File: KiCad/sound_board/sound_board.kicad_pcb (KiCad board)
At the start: 2 copper layers, 67.3 x 29.2 mm, 16 parts, among them P101 CONN_01X06, P102 CONN_01X06, P103 CONN_01X06, U101 MCP45HVx1, U102 MCP45HVx1, U103 DS1808

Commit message: Gerber
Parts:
- moved REF** 66.0 mm to (205.7, 109.2)
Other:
- board size 67.3 x 29.2 mm -> 65.4 x 26.7 mm
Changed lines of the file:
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@@
     (links 61)
     (no_connects 0)
-    (area 134.544999 93.904999 202.005001 123.265001)
+    (area 142.286667 86.265 221.233334 121.575)
     (thickness 1.6)
     (drawings 6)
@@
     (descr "Through hole straight pin header, 1x06, 2.54mm pitch, single row")
     (tags "Through hole pin header THT 1x06 2.54mm single row")
-    (fp_text reference P103 (at 0 2.39 270) (layer B.SilkS)
+    (fp_text reference P103 (at 0 -15.24 270) (layer B.SilkS)
       (effects (font (size 1 1) (thickness 0.15)) (justify mirror))
     )
@@
   )
   (module Mounting_Holes:MountingHole_3.2mm_M3_Pad (layer F.Cu)
-    (at 139.7 109.22)
+    (at 205.74 109.22)
     (descr "Mounting Hole 3.2mm, M3")
     (tags "mounting hole 3.2mm m3")
@@
     (pad 1 thru_hole circle (at 0 0) (size 6.4 6.4) (drill 3.2) (layers *.Cu *.Mask))
   )
-  (dimension 67.31 (width 0.25) (layer Cmts.User)
-    (gr_text "67,310 mm" (at 168.275 129.27) (layer Cmts.User)
+  (dimension 65.405 (width 0.25) (layer Cmts.User)
+    (gr_text "65,405 mm" (at 176.8475 87.265) (layer Cmts.User)
       (effects (font (size 1 1) (thickness 0.25)))
     )
-    (feature1 (pts (xy 201.93 123.19) (xy 201.93 130.27)))
-    (feature2 (pts (xy 134.62 123.19) (xy 134.62 130.27)))
-    (crossbar (pts (xy 134.62 128.27) (xy 201.93 128.27)))
-    (arrow1a (pts (xy 201.93 128.27) (xy 200.803496 128.856421)))
-    (arrow1b (pts (xy 201.93 128.27) (xy 200.803496 127.683579)))
-    (arrow2a (pts (xy 134.62 128.27) (xy 135.746504 128.856421)))
-    (arrow2b (pts (xy 134.62 128.27) (xy 135.746504 127.683579)))
-  )
-  (dimension 29.21 (width 0.25) (layer Cmts.User)
-    (gr_text "29,210 mm" (at 208.01 108.585 270) (layer Cmts.User)
+    (feature1 (pts (xy 209.55 94.615) (xy 209.55 86.265)))
+    (feature2 (pts (xy 144.145 94.615) (xy 144.145 86.265)))
+    (crossbar (pts (xy 144.145 88.265) (xy 209.55 88.265)))
+    (arrow1a (pts (xy 209.55 88.265) (xy 208.423496 88.851421)))
+    (arrow1b (pts (xy 209.55 88.265) (xy 208.423496 87.678579)))
+    (arrow2a (pts (xy 144.145 88.265) (xy 145.271504 88.851421)))
+    (arrow2b (pts (xy 144.145 88.265) (xy 145.271504 87.678579)))
+  )
+  (dimension 26.67 (width 0.25) (layer Cmts.User)
+    (gr_text "26,670 mm" (at 216.9 107.95 270) (layer Cmts.User)
       (effects (font (size 1 1) (thickness 0.25)))
     )
-    (feature1 (pts (xy 201.93 123.19) (xy 209.01 123.19)))
-    (feature2 (pts (xy 201.93 93.98) (xy 209.01 93.98)))
-    (crossbar (pts (xy 207.01 93.98) (xy 207.01 123.19)))
-    (arrow1a (pts (xy 207.01 123.19) (xy 206.423579 122.063496)))
-    (arrow1b (pts (xy 207.01 123.19) (xy 207.596421 122.063496)))
-    (arrow2a (pts (xy 207.01 93.98) (xy 206.423579 95.106504)))
-    (arrow2b (pts (xy 207.01 93.98) (xy 207.596421 95.106504)))
-  )
-  (gr_line (start 134.62 123.19) (end 134.62 93.98) (angle 90) (layer Edge.Cuts) (width 0.15))
-  (gr_line (start 201.93 123.19) (end 134.62 123.19) (angle 90) (layer Edge.Cuts) (width 0.15))
-  (gr_line (start 201.93 93.98) (end 201.93 123.19) (angle 90) (layer Edge.Cuts) (width 0.15))
-  (gr_line (start 134.62 93.98) (end 201.93 93.98) (angle 90) (layer Edge.Cuts) (width 0.15))
+    (feature1 (pts (xy 209.55 121.285) (xy 217.9 121.285)))
+    (feature2 (pts (xy 209.55 94.615) (xy 217.9 94.615)))
+    (crossbar (pts (xy 215.9 94.615) (xy 215.9 121.285)))
+    (arrow1a (pts (xy 215.9 121.285) (xy 215.313579 120.158496)))
+    (arrow1b (pts (xy 215.9 121.285) (xy 216.486421 120.158496)))
+    (arrow2a (pts (xy 215.9 94.615) (xy 215.313579 95.741504)))
+    (arrow2b (pts (xy 215.9 94.615) (xy 216.486421 95.741504)))
+  )
+  (gr_line (start 144.145 121.285) (end 144.145 94.615) (angle 90) (layer Edge.Cuts) (width 0.15))
+  (gr_line (start 209.55 121.285) (end 144.145 121.285) (angle 90) (layer Edge.Cuts) (width 0.15))
+  (gr_line (start 209.55 94.615) (end 209.55 121.285) (angle 90) (layer Edge.Cuts) (width 0.15))
+  (gr_line (start 144.145 94.615) (end 209.55 94.615) (angle 90) (layer Edge.Cuts) (width 0.15))
   (segment (start 149.86 107.95) (end 147.32 107.95) (width 0.25) (layer F.Cu) (net 1))
   (segment (start 147.32 107.95) (end 145.542 109.728) (width 0.25) (layer F.Cu) (net 1))
@@
     (polygon
       (pts
-        (xy 134.62 93.98) (xy 201.93 93.98) (xy 201.93 123.19) (xy 134.62 123.19)
+        (xy 144.145 94.615) (xy 209.55 94.615) (xy 209.55 121.285) (xy 144.145 121.285)
       )
     )
@@
     (polygon
       (pts
-        (xy 134.62 123.19) (xy 134.62 93.98) (xy 201.93 93.98) (xy 201.93 123.19)
+        (xy 209.55 94.615) (xy 209.55 121.285) (xy 144.145 121.285) (xy 144.145 94.615)
       )
     )

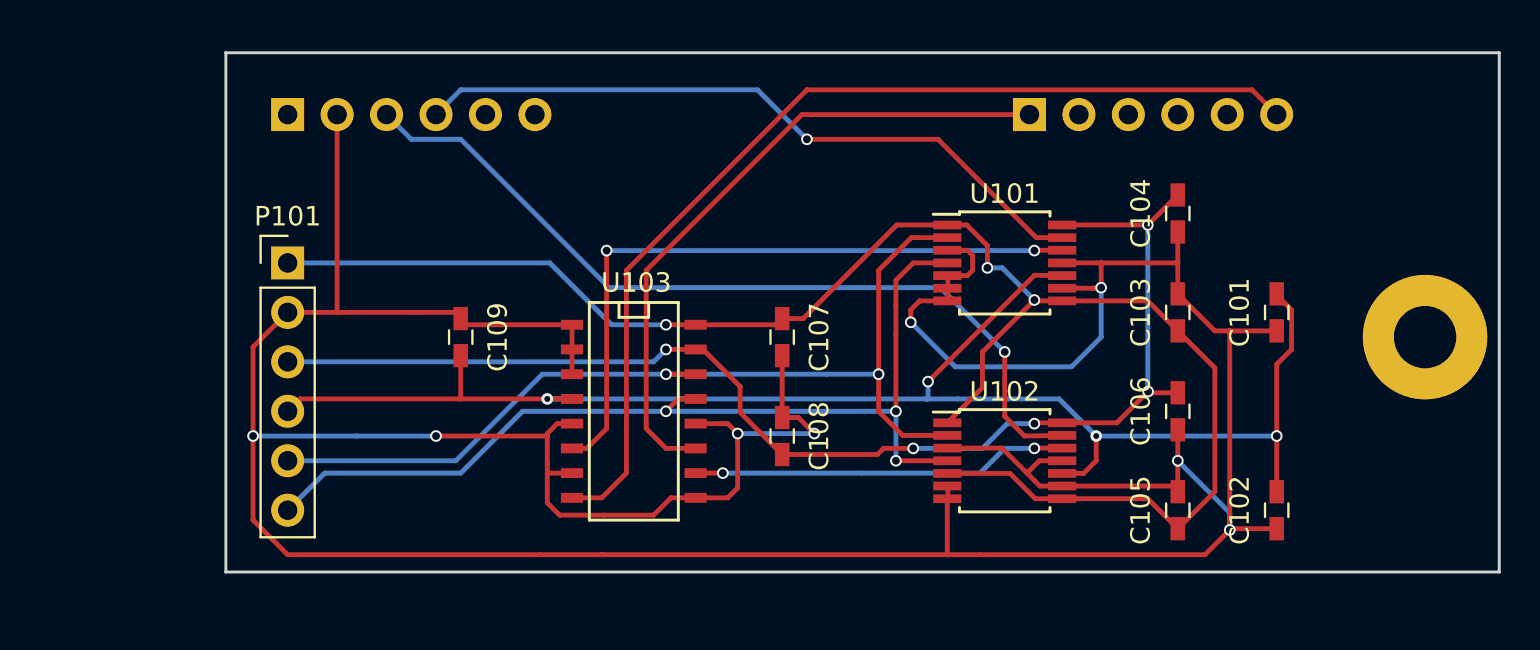
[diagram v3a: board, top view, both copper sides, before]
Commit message: Only one i2c potentiometer to manage sound
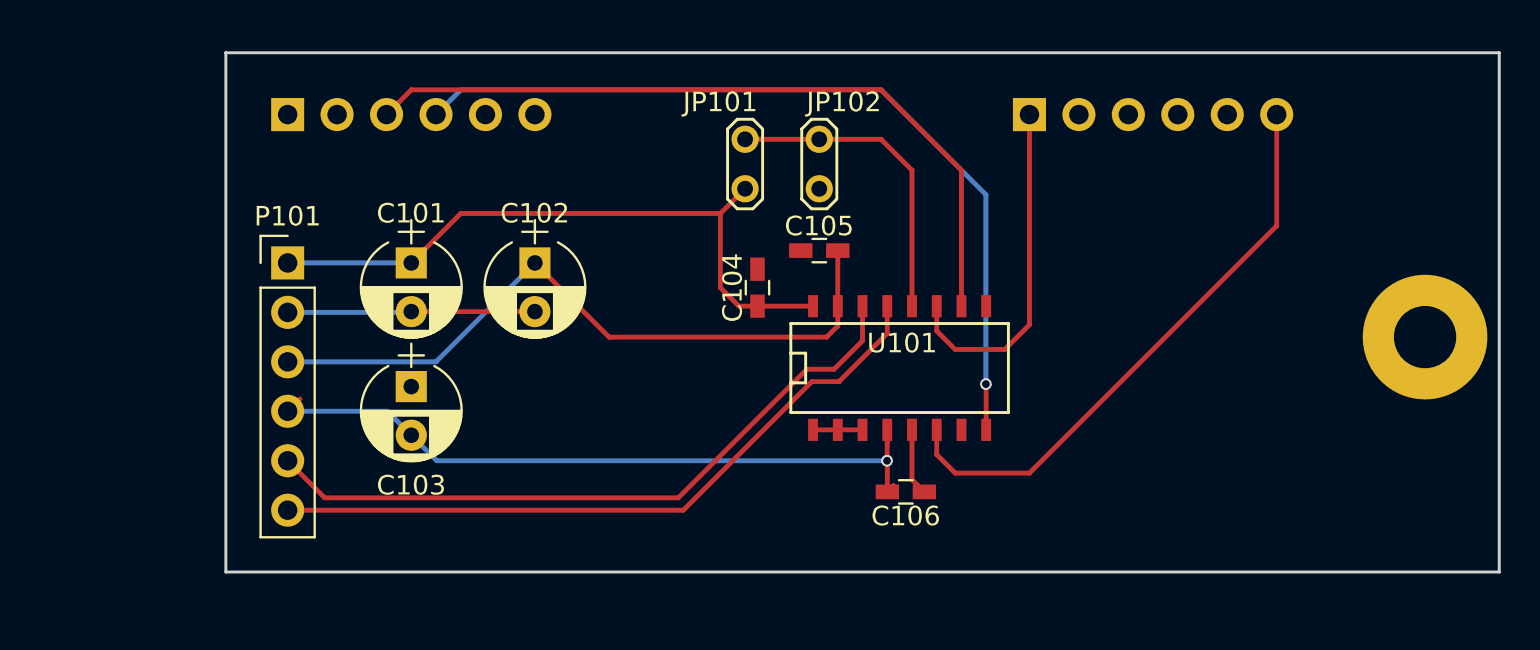
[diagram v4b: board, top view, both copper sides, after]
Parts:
- removed C107, C108, C109: 100nF, Capacitors_SMD:C_0603_HandSoldering
- removed U102: MCP45HVx1, Housings_SSOP:TSSOP-14_4.4x5mm_Pitch0.65mm
- removed U103: DS1808, SMD_Packages:SO-16-N
- added JP101: Jumper, Measurement_Points:Test_Point_2Pads, F.Cu at (170.8, 99.1)
- added JP102: Jumper, Measurement_Points:Test_Point_2Pads, F.Cu at (174.6, 101.6)
- C101, C102, C103: value 100nF -> 10uF; footprint Capacitors_SMD:C_0603_HandSoldering -> Capacitors_ThroughHole:CP_Radial_D5.0mm_P2.50mm
- U101: value MCP45HVx1 -> DS1808; footprint Housings_SSOP:TSSOP-14_4.4x5mm_Pitch0.65mm -> SMD_Packages:SO-16-N
- moved C101 44.5 mm to (153.7, 105.4), turned to 270 degrees
- moved C102 40.2 mm to (160.0, 105.4), turned to 270 degrees
- moved C103 39.6 mm to (153.7, 111.8)
- moved C105 22.7 mm to (174.6, 104.8), turned to 0 degrees
- moved C104 21.9 mm to (171.4, 106.7), turned to 270 degrees
- moved C106 14.6 mm to (179.1, 117.2), turned to 180 degrees
- moved U101 7.63 mm to (178.8, 110.8)
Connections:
- C101 pad 1: GND -> +5V
- C101 pad 2: -7.2V -> GND
- C102 pad 1: GND -> +7.2V
- C102 pad 2: -7.2V -> GND
- C103 pad 2: +5V -> -7.2V
- C104 pad 2: +7.2V -> +5V
- C105 pad 2: +5V -> +7.2V
- C106 pad 2: +7.2V -> -7.2V
- U101 pad 1: +5V -> GND
- U101 pad 10: -7.2V -> /BAL_HIGH_L
- U101 pad 11: GND -> /VOL_WIPPER_L
- U101 pad 13: /BAL_HIGH_R -> /I2C-SDA
- U101 pad 14: +7.2V -> /I2C-SCL
- U101 pad 2: /I2C-SCL -> GND
- U101 pad 4: /I2C-SDA -> -7.2V
- U101 pad 6: GND -> /VOL_WIPPER_R
- U101 pad 8: +5V -> /BAL_HIGH_R
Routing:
- net GND: track 218.7 -> 19.2 mm, vias 8 -> 0
- net +5V: track 85.8 -> 34.0 mm, vias 3 -> 0
- net -7.2V: track 80.3 -> 36.8 mm, vias 4 -> 1
- net +7.2V: track 66.7 -> 36.1 mm, vias 5 -> 0
- net /VOL_WIPPER_R: track 52.3 -> 30.1 mm
- net Net-(U102-Pad12): track 19.4 -> 0.00 mm, vias 2 -> 0
- net Net-(JP101-Pad1): track 34.8 -> 16.2 mm, vias 2 -> 0
- net /VOL_WIPPER_L: track 34.3 -> 17.7 mm
- net /I2C-SDA: track 50.4 -> 36.0 mm, vias 3 -> 0
- net /I2C-SCL: track 49.3 -> 35.4 mm, vias 2 -> 0
- net /BAL_HIGH_R: track 35.9 -> 43.1 mm
- net /BAL_HIGH_L: track 43.5 -> 38.7 mm, vias 1 -> 0
